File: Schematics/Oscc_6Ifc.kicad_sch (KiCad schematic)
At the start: 95 parts, among them J32 Conn_01x10h, J33 Conn_01x10h, J34 Conn_01x12, J35 Conn_01x12, J36 Conn_01x10h, J37 Conn_01x10h, J38 Conn_01x12, J39 Conn_01x12, J40 Conn_01x10h, J41 Conn_01x04, J42 Conn_01x04, J43 Conn_01x12, J44 Conn_01x10h, J45 Conn_01x12, P2 Conn_01x03, U85 LMT358N, U86 LM358, U87 LM358, U88 LMT358N, U89 LM358, U90 LMT358N, U91 LMT358N, U92 LM358, U93 LM358, U94 LMT358N, U95 LM358, U96 LMT358N, U97 LM78L05

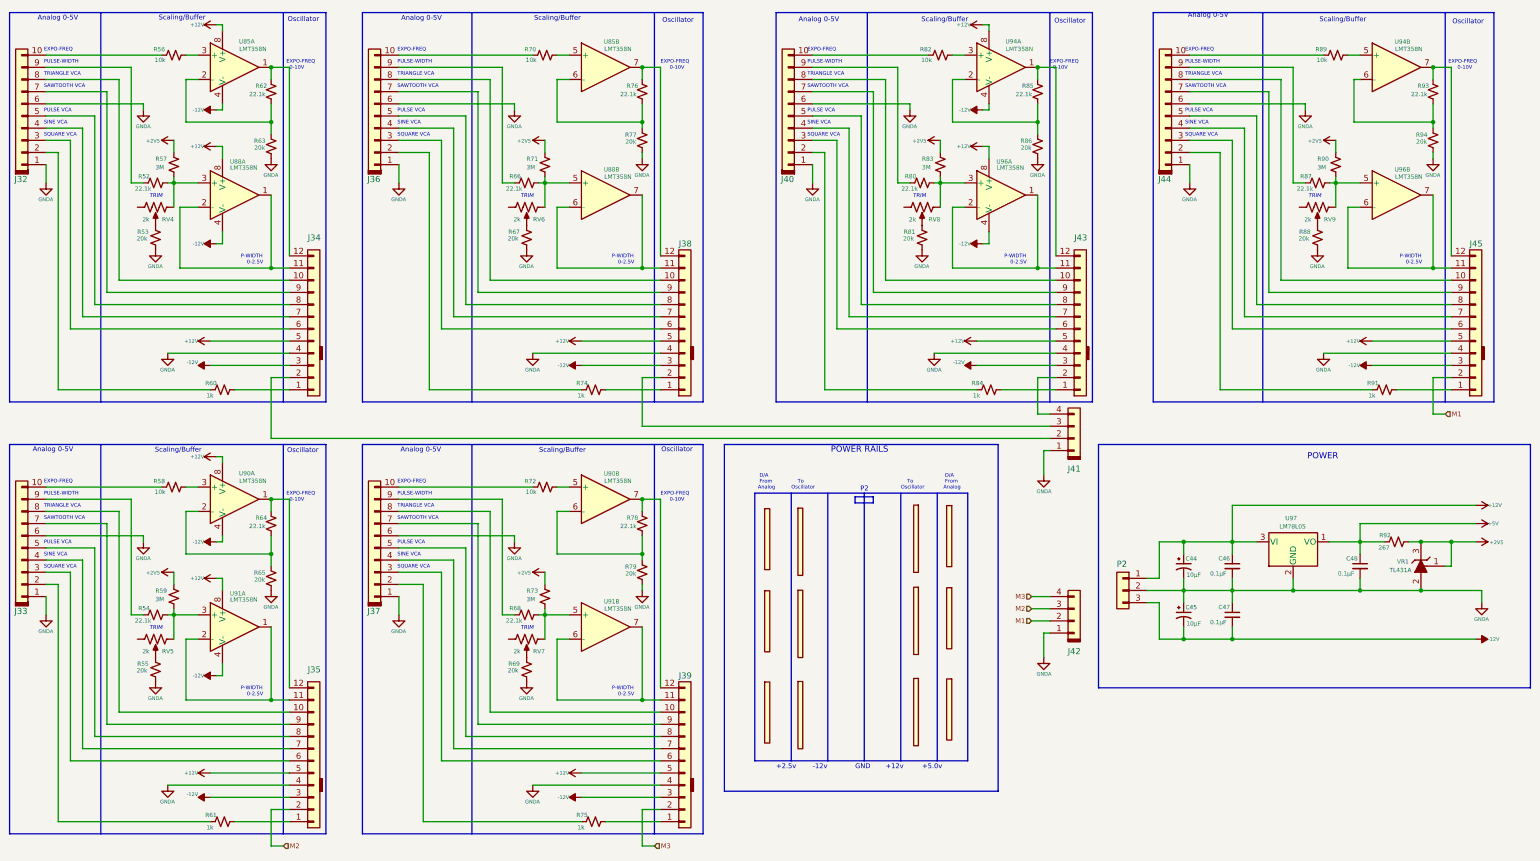
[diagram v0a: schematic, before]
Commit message: Now with dual ESP32 with Midi32 and Disp32.
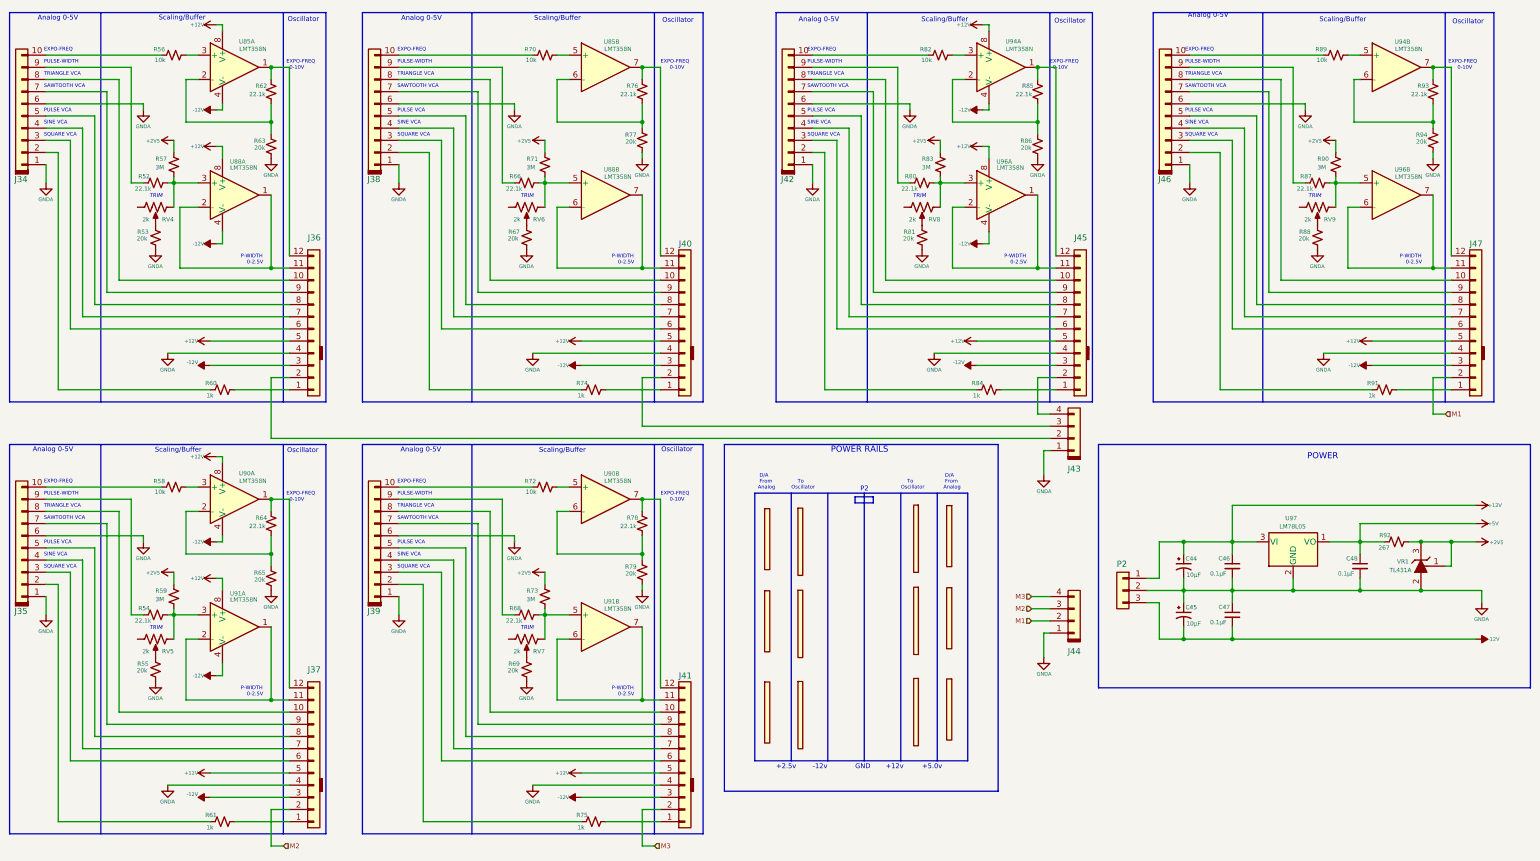
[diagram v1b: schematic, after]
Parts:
- renumbered J32 to J34, J33 to J35, J34 to J36, J35 to J37, J36 to J38, J37 to J39, J38 to J40, J39 to J41, J40 to J42, J41 to J43, J42 to J44, J43 to J45, J44 to J46, J45 to J47
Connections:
- net at RV4. (3): now also R53.1
- net at RV8. (3): now also R81.1

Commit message: Disp32 interface working properly.
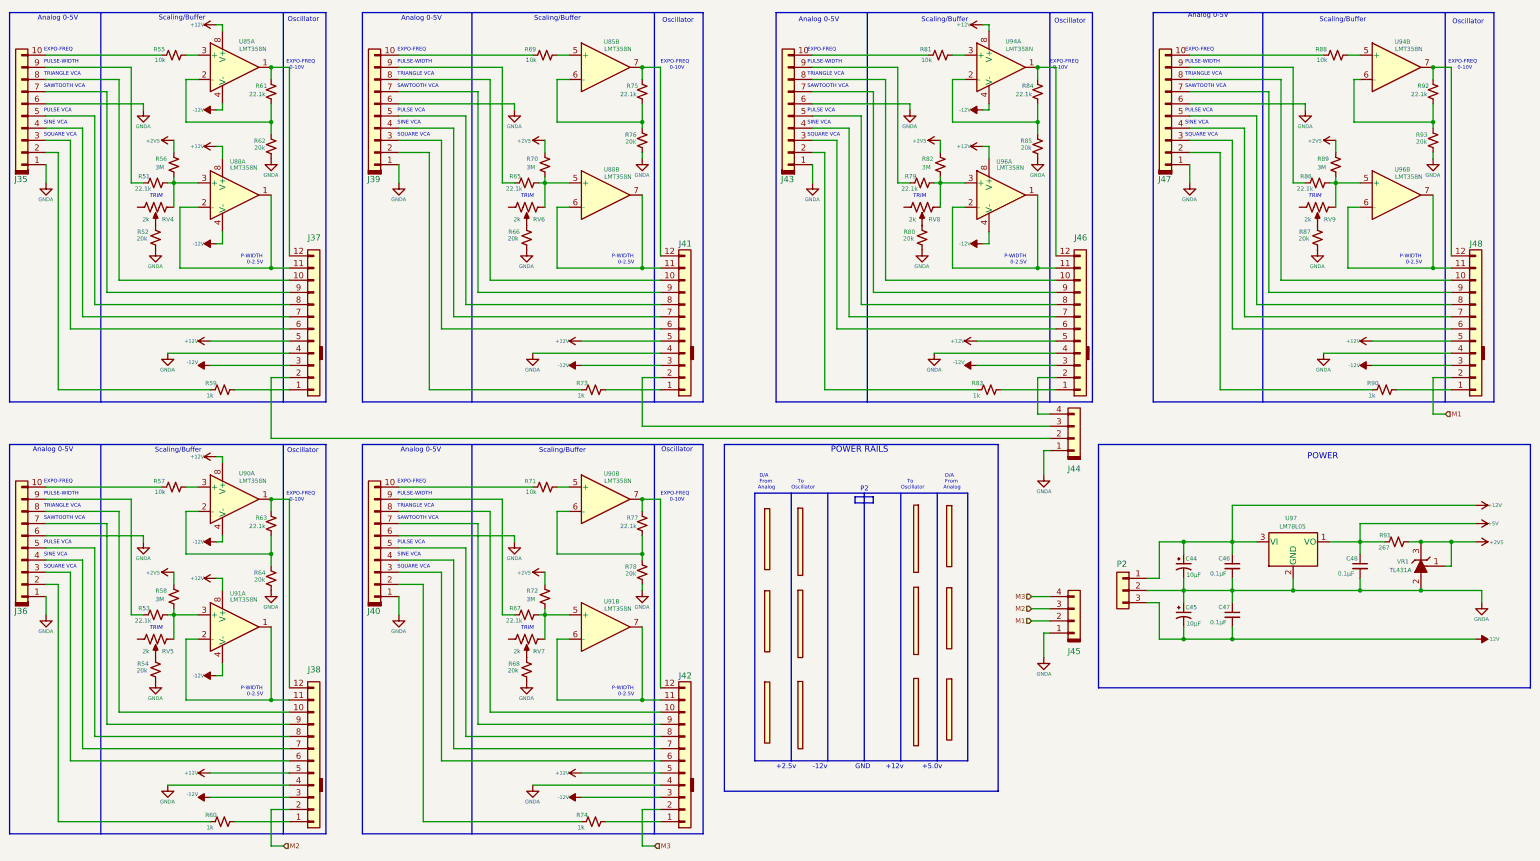
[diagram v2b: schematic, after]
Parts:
- renumbered J34 to J35, J35 to J36, J36 to J37, J37 to J38, J38 to J39, J39 to J40, J40 to J41, J41 to J42, J42 to J43, J43 to J44, J44 to J45, J45 to J46, J46 to J47, J47 to J48, R52 to R51, R53 to R52, R54 to R53, R55 to R54, R56 to R55, R57 to R56, R58 to R57, R59 to R58, R60 to R59, R61 to R60, R62 to R61, R63 to R62, R64 to R63, R65 to R64, R66 to R65, R67 to R66, R68 to R67, R69 to R68, R70 to R69, R71 to R70, R72 to R71, R73 to R72, R74 to R73, R75 to R74, R76 to R75, R77 to R76, R78 to R77, R79 to R78, R80 to R79, R81 to R80, R82 to R81, R83 to R82, R84 to R83, R85 to R84, R86 to R85, R87 to R86, R88 to R87, R89 to R88, R90 to R89, R91 to R90, R92 to R91, R93 to R92, R94 to R93
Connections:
- net at RV4. (3): now also R52.1
- net at RV8. (3): now also R80.1

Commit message: Noise generator and experimental steups.
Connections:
- net at RV4. (3): now also R52.1
- net at RV8. (3): now also R80.1

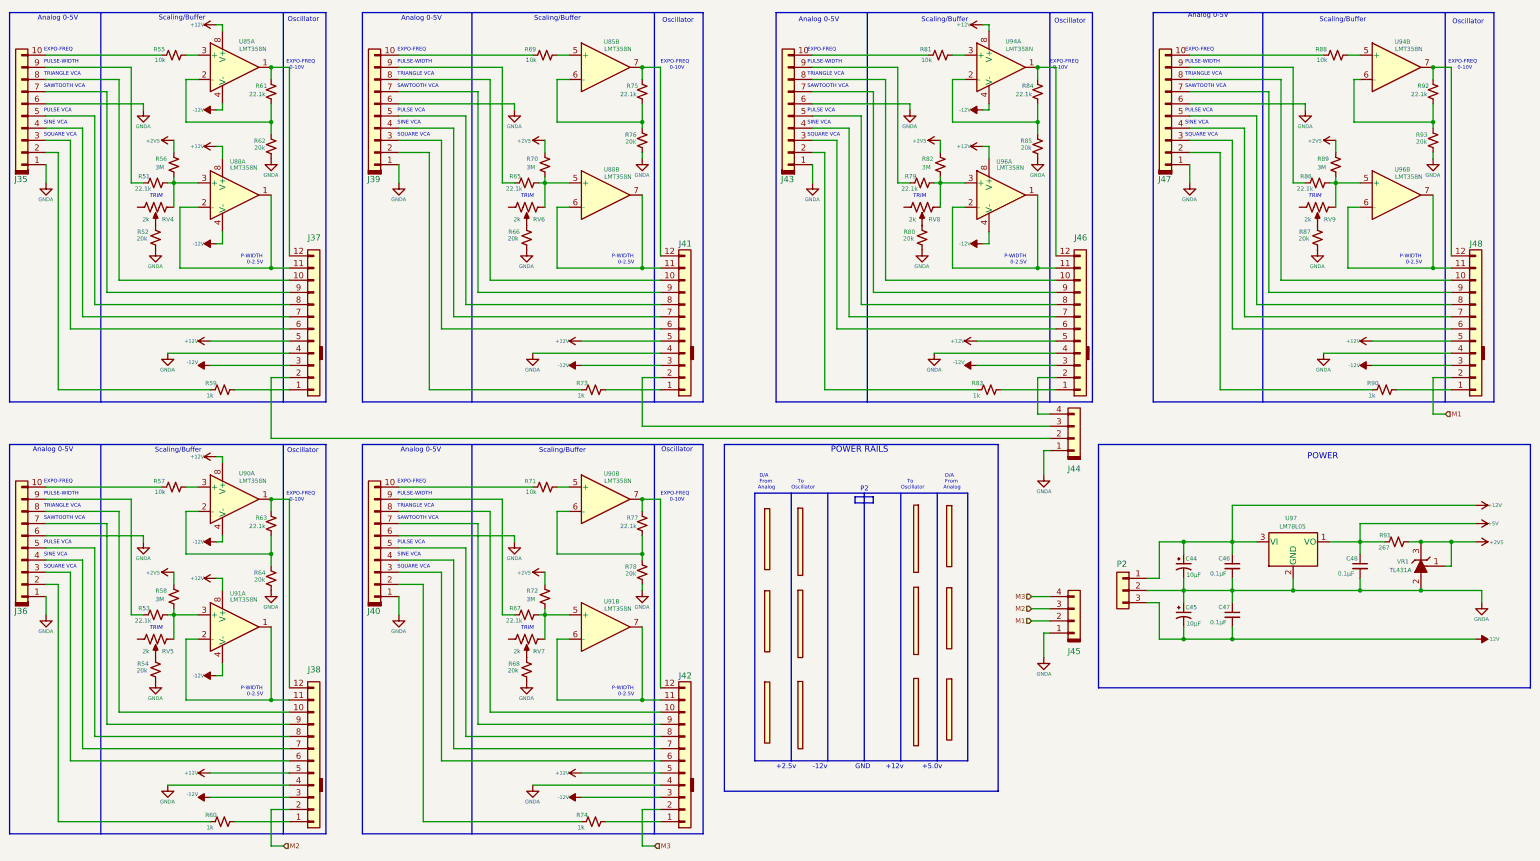
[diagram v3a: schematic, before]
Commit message: adding noise source and variable state filter.
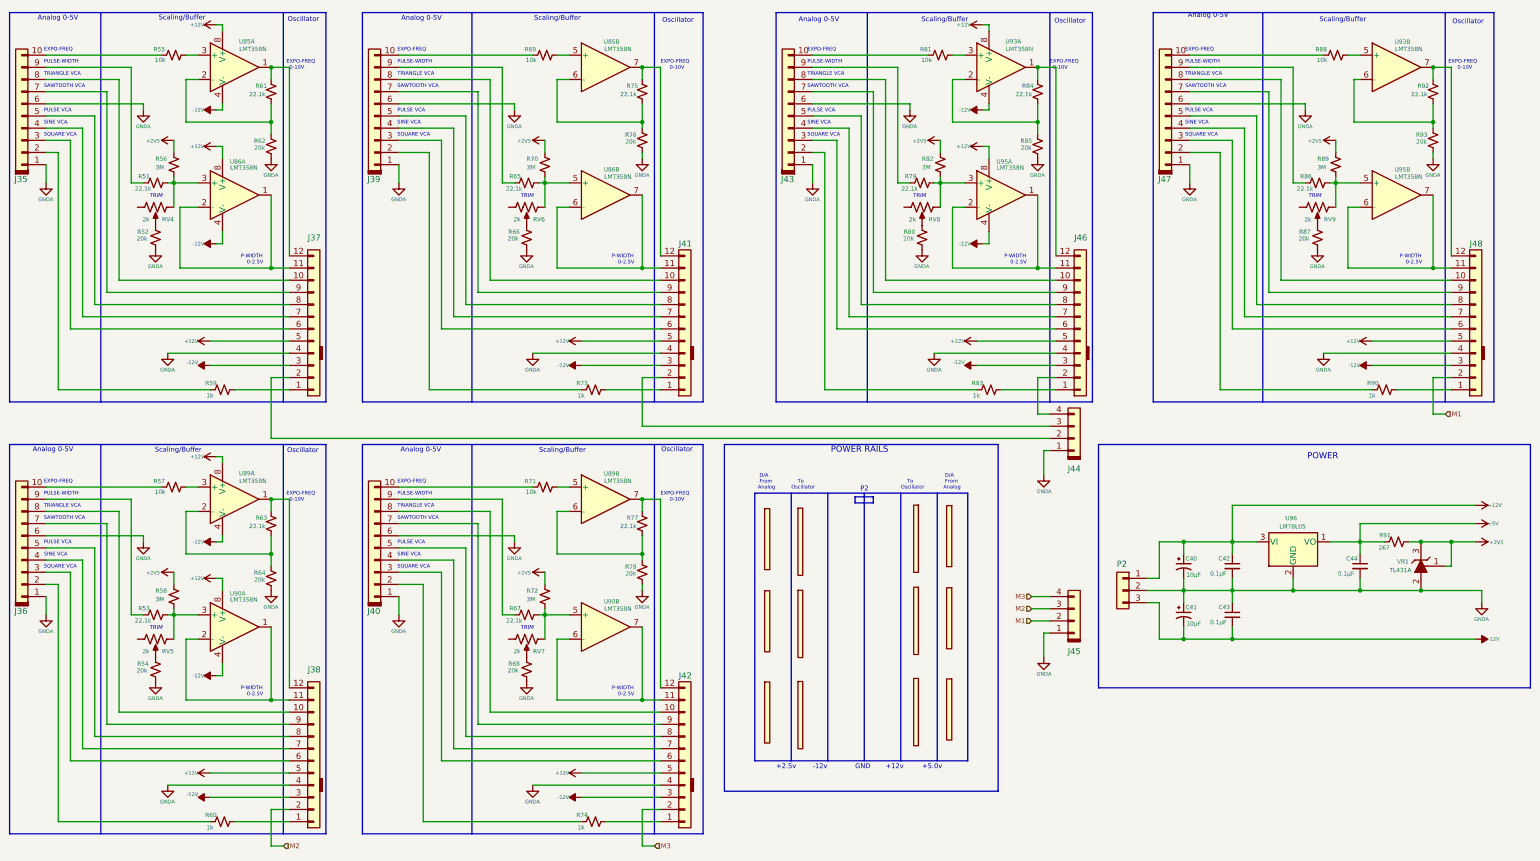
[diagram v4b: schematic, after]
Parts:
- removed C44, C45: 10µF, symbol Device:C_Polarized_Small_US
- removed C46, C47, C48: 0.1µF, symbol Device:C_Small
- removed U86: LM358, symbol Amplifier_Operational:LM358
- removed U88: LMT358N, symbol Amplifier_Operational:LM358
- removed U97: LM78L05, Package_TO_SOT_THT:TO-92_Inline, symbol Regulator_Linear:LM78L05_TO92
- added C40, C41: 10µF, symbol Device:C_Polarized_Small_US
- added C42, C43, C44: 0.1µF, symbol Device:C_Small
- added U84: LM358, symbol Amplifier_Operational:LM358
- added U86: LMT358N, symbol Amplifier_Operational:LM358
- added U96: LM78L05, Package_TO_SOT_THT:TO-92_Inline, symbol Regulator_Linear:LM78L05_TO92
- renumbered U89 to U88, U90 to U89, U91 to U90, U92 to U91, U93 to U92, U94 to U93, U95 to U94, U96 to U95
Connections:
- net +12V: now also C40.1, C42.1, U84.8 (V+), U96.3 (VI)
- net +5V: now also C44.1, U96.1 (VO)
- net -12V: now also C41.2, C43.2, U84.4 (V-)
- net GNDA: now also C40.2, C41.1, C42.2, C43.1, C44.2, U96.2 (GND)
- net at R65.2, R70.2, RV6. (3): now also U86.5 (+)
- net at R51.2, R56.2, RV4. (3): now also U86.3 (+)
- net at RV4. (3): now also R52.1
- net at J41.11 (Pin_11): now also U86.6 (-), U86.7
- net at J37.11 (Pin_11): now also U86.1, U86.2 (-)
- net at RV8. (3): now also R80.1

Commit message: Noise boards added.
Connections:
- net at RV4. (3): now also R52.1
- net at RV6. (3): now also R66.1
- net at RV8. (3): now also R80.1

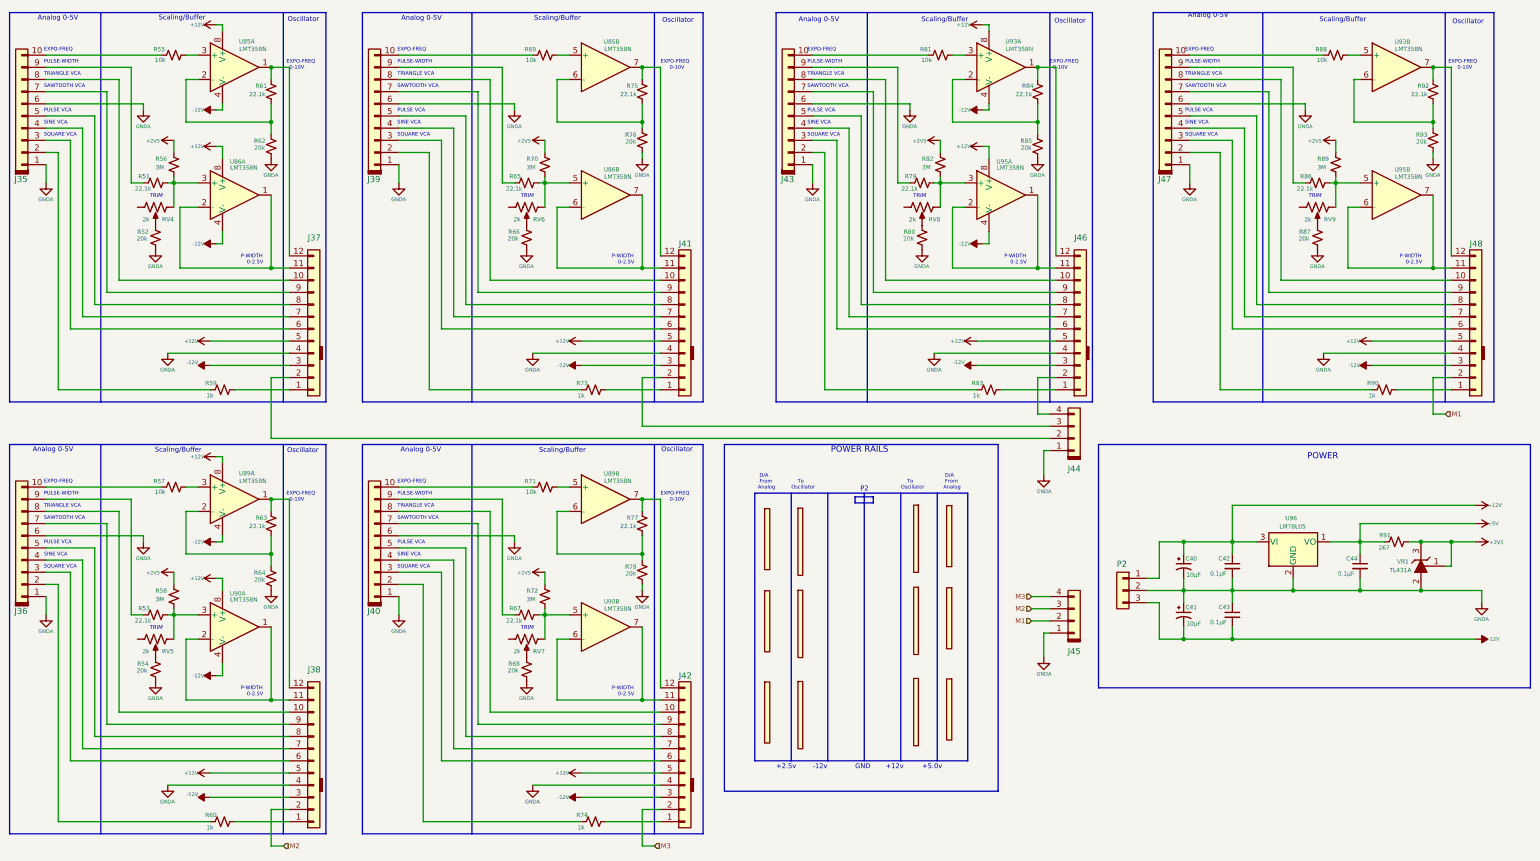
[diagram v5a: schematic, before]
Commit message: Update with noise filter & VCA as well as envelope generator software shell.
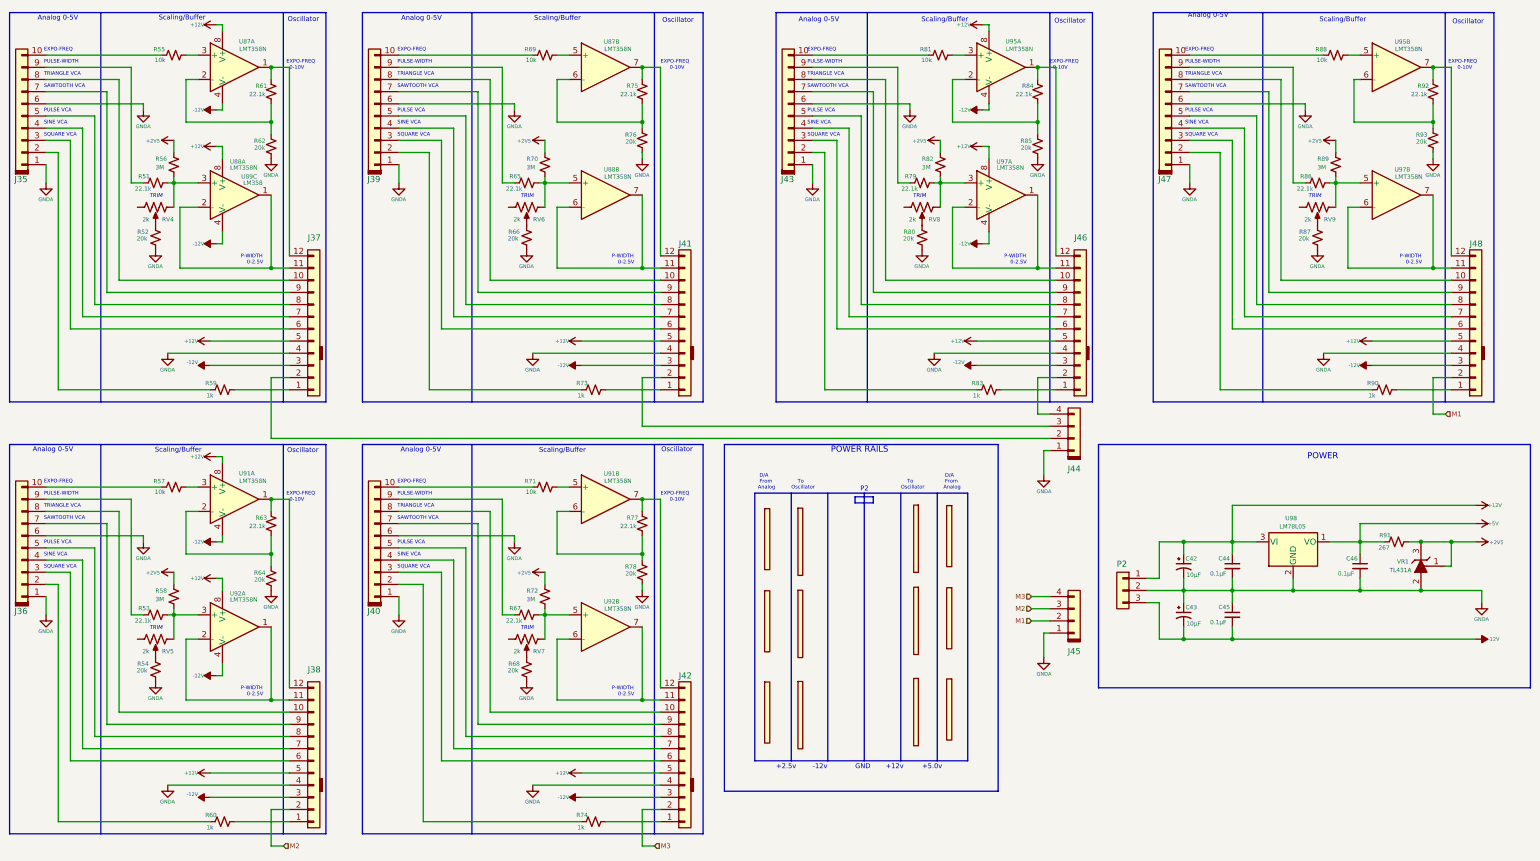
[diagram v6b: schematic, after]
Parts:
- renumbered C40 to C42, C41 to C43, C42 to C44, C43 to C45, C44 to C46, U84 to U86, U85 to U87, U86 to U88, U87 to U89, U88 to U90, U89 to U91, U90 to U92, U91 to U93, U92 to U94, U93 to U95, U94 to U96, U95 to U97, U96 to U98
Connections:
- net at RV4. (3): now also R52.1
- net at RV6. (3): now also R66.1
- net at RV8. (3): now also R80.1

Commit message: sync up first noise board.
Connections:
- net at RV4. (3): now also R52.1
- net at RV6. (3): now also R66.1
- net at RV8. (3): now also R80.1
